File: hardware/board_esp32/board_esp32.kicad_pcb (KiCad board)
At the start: 2 copper layers, 93 parts, among them J1 USB_B_Micro, J2 Conn_01x02, J3 Micro_SD_Card_Det_Hirose_DM3AT, Q1 AO3401, Q2 AO3400, Q3 AO3401, SW1 SW_Push, U1 FT231XS, U2 ESP32-WROOM-32D, U3 E22-900M22S, U4 E22-900M30S, U5 TPS62162DGK

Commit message: adds changelog and pcb components are organised
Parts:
- removed C11: NC, Capacitor_SMD:C_0805_2012Metric
- moved Q2 131.8 mm to (255.5, 71.2), turned to 90 degrees
- moved J2 73.4 mm to (265.0, 66.0)
- moved J1 67.9 mm to (261.8, 50.5), turned to 90 degrees
- moved C1 62.6 mm to (256.2, 49.0), turned to 90 degrees
- moved C2 62.2 mm to (256.2, 51.2), turned to -90 degrees
- moved D1 61.4 mm to (257.5, 51.2), turned to -90 degrees
- moved R2 61.0 mm to (254.5, 50.8)
- moved R1 60.9 mm to (254.5, 49.5)
- moved Q3 59.6 mm to (259.5, 67.2)
- moved R6 59.4 mm to (256.5, 67.7), turned to 90 degrees
- moved D3 58.9 mm to (257.5, 53.5), turned to -90 degrees
- moved D2 58.6 mm to (257.5, 49.0)
- moved JP3 58.5 mm to (237.5, 46.0)
- moved JP4 57.9 mm to (237.5, 43.0)
- moved Q1 57.8 mm to (252.5, 67.2)
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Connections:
- SW1 pad 2: GND -> /SW_RESET

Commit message: finishes placement and starts routing
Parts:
- added H1: MountingHole_Pad, MountingHole:MountingHole_2.2mm_M2, F.Cu at (13.0, 13.0)
- added H2: MountingHole_Pad, MountingHole:MountingHole_2.2mm_M2, F.Cu at (62.0, 87.0)
- added H3: MountingHole_Pad, MountingHole:MountingHole_2.2mm_M2, F.Cu at (13.0, 87.0)
- added H4: MountingHole_Pad, MountingHole:MountingHole_2.2mm_M2, F.Cu at (62.0, 13.0)
- JP10, JP11, JP12, JP15, JP16, JP17, JP18, JP19, JP2, JP20, JP21, JP22, JP23, JP24, JP26, JP27, JP28, JP29, JP3, JP30, JP31, JP32, JP33, JP4, JP5, JP6, JP7, JP8, JP9, TP1, TP2, TP3, TP4: moved to B.Cu
- moved D5 232.9 mm to (13.0, 19.0), turned to 180 degrees
- moved R12 229.0 mm to (16.0, 19.0), turned to 0 degrees
- moved D4 228.8 mm to (13.0, 25.0), turned to 180 degrees
- moved R11 225.0 mm to (16.0, 25.0), turned to 0 degrees
- moved D6 222.8 mm to (13.0, 60.0), turned to 180 degrees
- moved R15 219.3 mm to (16.0, 60.0), turned to 0 degrees
- moved JP2 206.6 mm to (46.0, 33.0), turned to 180 degrees
- moved J2 203.2 mm to (62.0, 58.0)
- moved C7 202.9 mm to (52.5, 55.5)
- moved Q1 202.9 mm to (50.0, 55.0)
- moved Q2 202.9 mm to (53.0, 59.0)
- moved Q3 202.9 mm to (57.0, 55.0)
- moved R6 202.9 mm to (54.0, 55.5)
- moved R7 202.9 mm to (53.5, 53.5)
- moved J1 199.5 mm to (62.3, 45.0)
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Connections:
- SW1 pad 2: /SW_RESET -> GND
- U2 pad 10: /LORA1_RXEN -> /LORA1_TXEN
- U2 pad 12: /LORA1_TXEN -> /LORA1_RXEN
- U2 pad 27: /LORA1_DIO2 -> /LORA1_NSS
- U2 pad 33: /LORA1_NSS -> /LORA1_DIO2
- U2 pad 36: /LORA2_NSS -> /LORA1_BUSY
- U2 pad 6: /LORA1_BUSY -> /LORA2_NSS
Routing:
- net /LORA1_SCK: track 0.00 -> 54.7 mm, vias 0 -> 1
- net /LORA1_TXEN: track 0.00 -> 37.8 mm, vias 0 -> 1
- net /LORA1_RXEN: track 0.00 -> 37.2 mm, vias 0 -> 1
- net /ESP_LED: track 0.00 -> 28.5 mm
- net /FT_TXD: track 0.00 -> 21.7 mm, vias 0 -> 1
- net /LORA1_DIO1: track 0.00 -> 18.8 mm, vias 0 -> 1
- net /LORA1_DIO2: track 0.00 -> 18.6 mm, vias 0 -> 1
- net /FT_RXD: track 0.00 -> 15.5 mm, vias 0 -> 3
- net +3V3: track 0.00 -> 14.9 mm
- net /LORA1_MOSI: track 0.00 -> 12.6 mm, vias 0 -> 2
- net Net-(R13-Pad2): track 0.00 -> 10.8 mm
- net /LORA1_MISO: track 0.00 -> 9.51 mm, vias 0 -> 1
- net Net-(JP19-Pad2): track 0.00 -> 7.71 mm, vias 0 -> 1
- net /FT_DTR: track 0.00 -> 6.62 mm, vias 0 -> 1
- net Net-(JP18-Pad2): track 0.00 -> 5.71 mm, vias 0 -> 1
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- added copper zone on B.Cu, net GND
- added copper zone on F.Cu, net GND
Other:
- board outline added: 55 x 80 mm

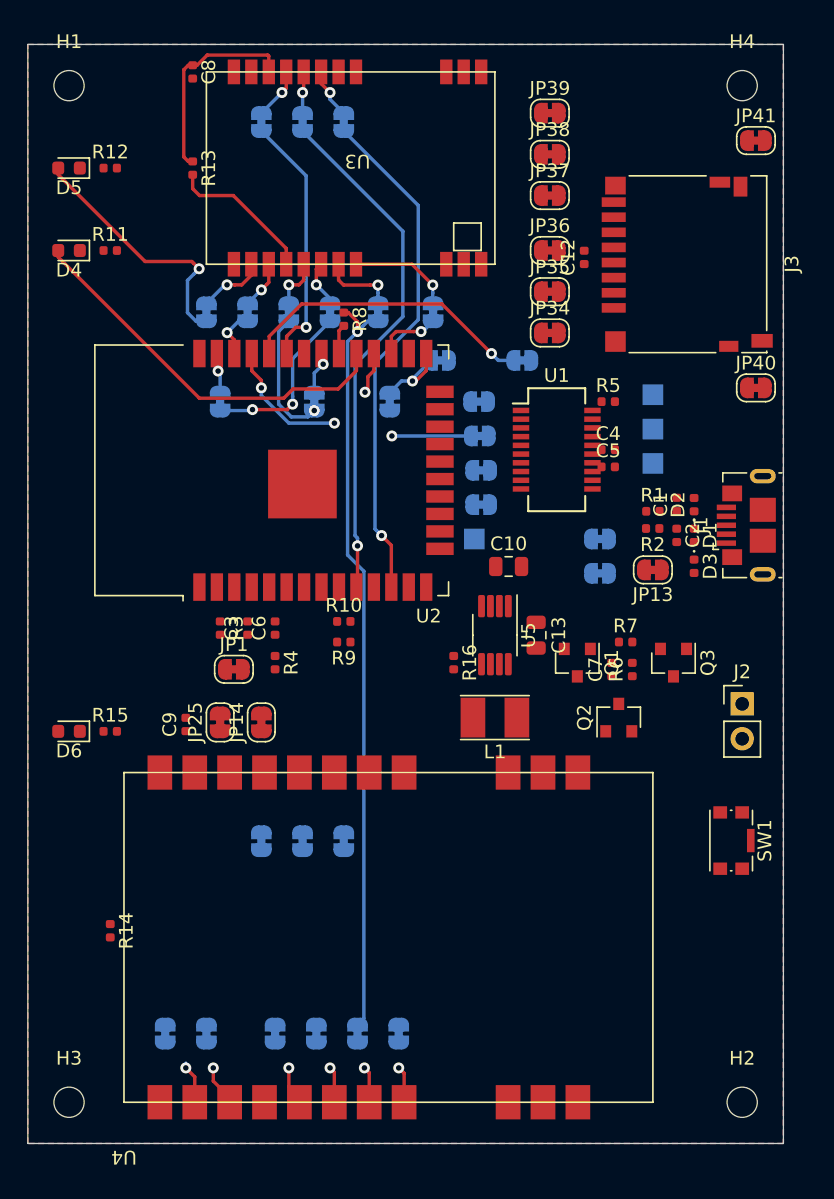
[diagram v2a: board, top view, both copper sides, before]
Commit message: finishes up layout of board_esp32
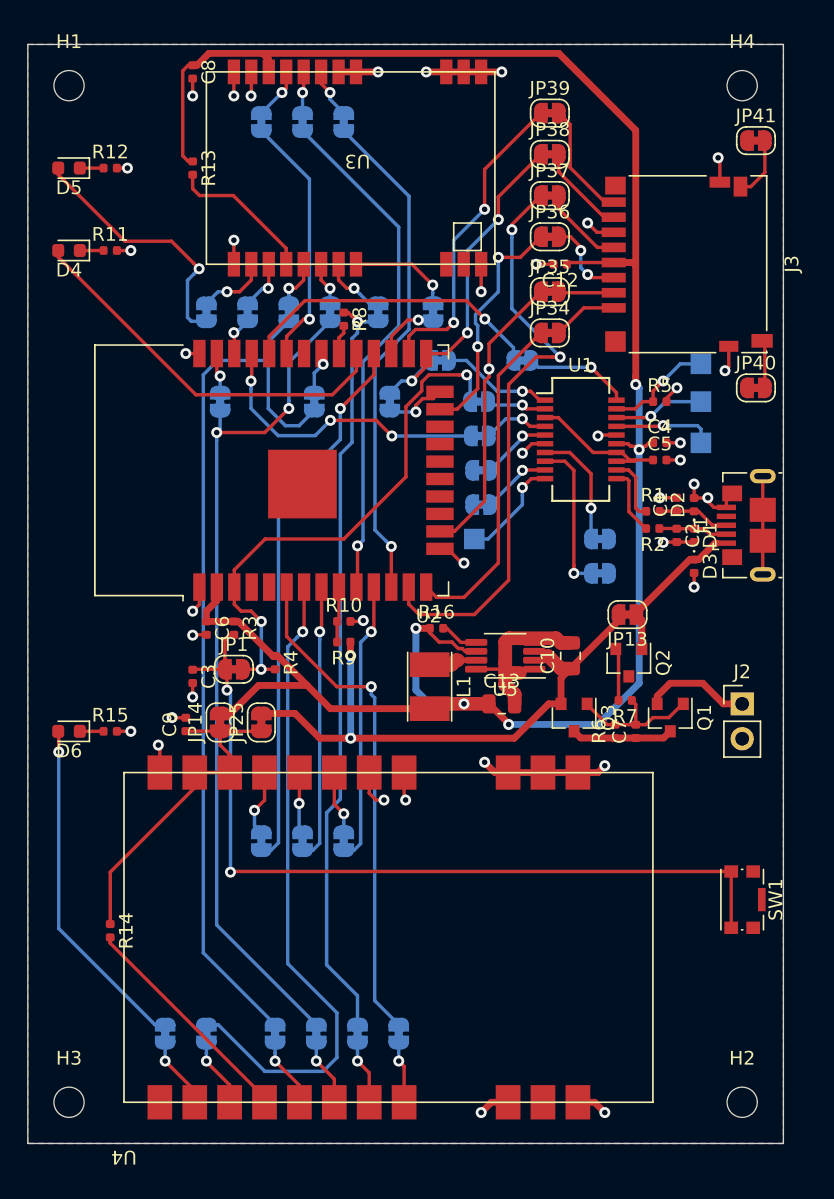
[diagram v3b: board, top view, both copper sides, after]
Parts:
- SW1: value SW_Push -> SW_Push-Std
- moved Q3 8.27 mm to (49.8, 59.0)
- moved TP4 8.05 mm to (59.0, 33.2)
- moved C10 7.91 mm to (49.5, 54.5), turned to 90 degrees
- moved Q1 7.86 mm to (56.8, 59.0)
- moved C13 5.59 mm to (44.5, 58.0), turned to 0 degrees
- moved C3 5.32 mm to (22.0, 56.0), turned to -90 degrees
- moved L1 5.26 mm to (39.2, 56.8), turned to -90 degrees
- moved C6 5.00 mm to (23.0, 52.5), turned to -90 degrees
- moved C7 4.83 mm to (54.2, 60.0)
- moved R6 4.67 mm to (52.8, 60.0)
- moved SW1 4.37 mm to (62.0, 72.2)
- moved R7 4.25 mm to (53.5, 57.8), turned to 180 degrees
- moved Q2 4.07 mm to (53.8, 55.0), turned to -90 degrees
- moved C4 3.78 mm to (56.0, 39.0)
- moved C5 3.78 mm to (56.0, 40.2)
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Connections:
- net Net-(C7-Pad1) renamed /BATT_PROT
- net Net-(J2-Pad1) renamed /BATT_IN
- J3 pad 11: Net-(J3-Pad11) -> GND
- SW1 pad 2: GND -> /SW_RESET
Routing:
- net +3V3: track 14.9 -> 152.9 mm, vias 0 -> 5
- net GND: track 0.00 -> 95.4 mm, vias 0 -> 39
- net /SW_RESET: track 0.00 -> 60.8 mm, vias 0 -> 2
- net /LORA1_MISO: track 9.51 -> 65.9 mm, vias 1 -> 0
- net /LORA1_MOSI: track 12.6 -> 61.4 mm
- net /LORA2_BUSY: track 0.00 -> 47.5 mm, vias 0 -> 1
- net /SD_CLK: track 0.00 -> 42.8 mm, vias 0 -> 2
- net +BATT: track 0.00 -> 41.4 mm, vias 0 -> 2
- net /FT_RTS: track 0.00 -> 39.0 mm, vias 0 -> 3
- net /LORA2_DIO2: track 3.08 -> 40.0 mm
- net /LORA2_NSS: track 0.00 -> 36.7 mm, vias 0 -> 1
- net /LORA2_DIO1: track 0.00 -> 25.0 mm, vias 0 -> 1
- net Net-(C9-Pad1): track 0.00 -> 24.9 mm
- net /SD_DAT2: track 0.00 -> 24.6 mm
- net /SD_DAT1: track 0.00 -> 22.8 mm, vias 0 -> 2
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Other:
- net class Default: clearance 0.2 -> 0.15
- net class PWR added: clearance 0.2, trace_width 0.25, via_dia 0.8, via_drill 0.4
- rule trace_clearance: 0.2 -> 0.15
- rule trace_min: 0.2 -> 0.15

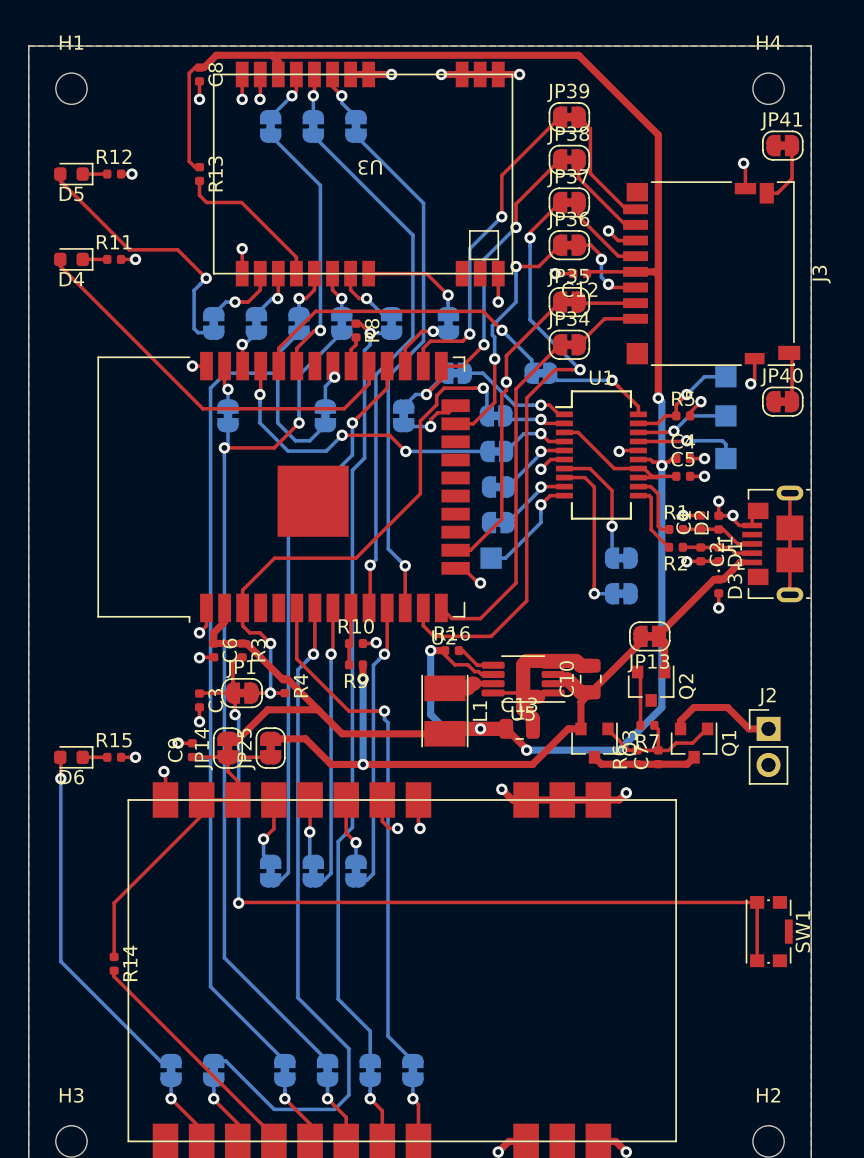
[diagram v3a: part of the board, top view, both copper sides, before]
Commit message: add a few more vias and generates GERBERs for board_esp32
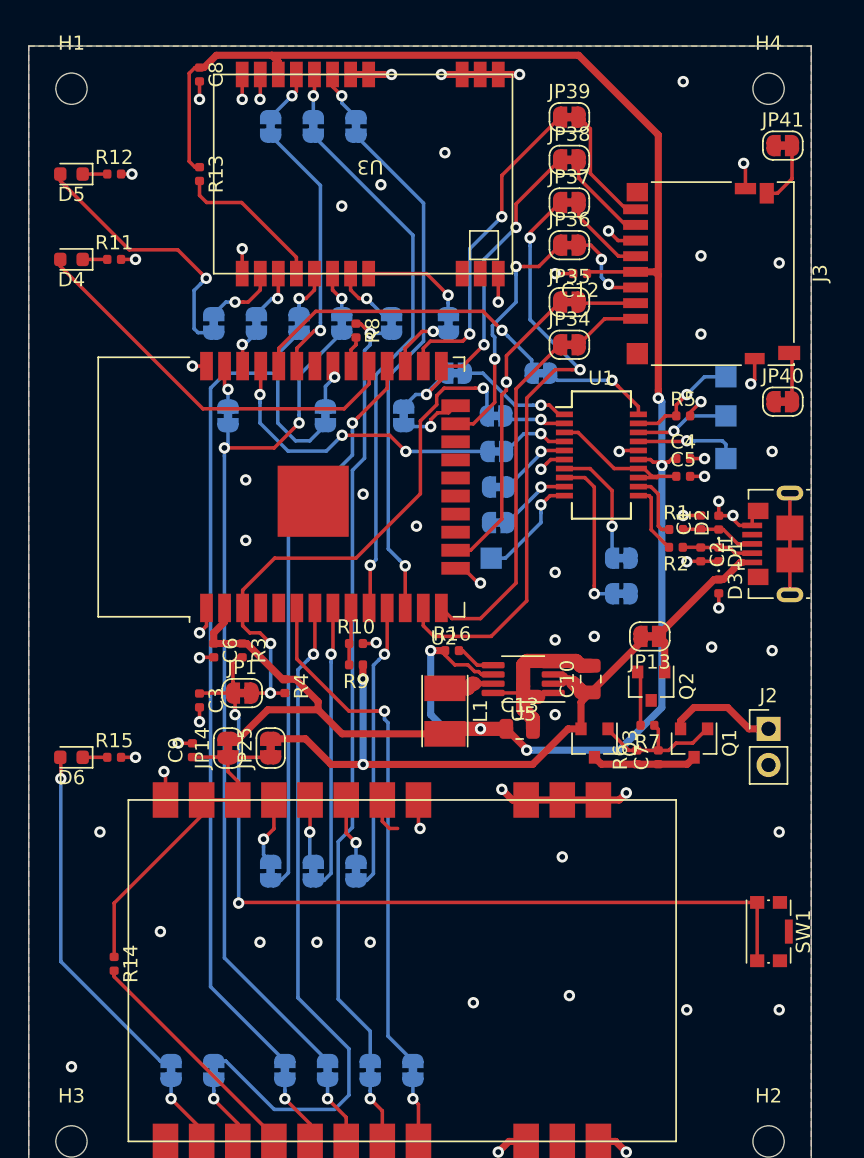
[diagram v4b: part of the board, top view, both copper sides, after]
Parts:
- U5: footprint Package_SO:MSOP-8_3x3mm_P0.65mm -> parts:MSOP-8_3x3mm_P0.65mm
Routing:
- net +BATT: track 41.4 -> 45.1 mm
- net GND: vias 39 -> 68

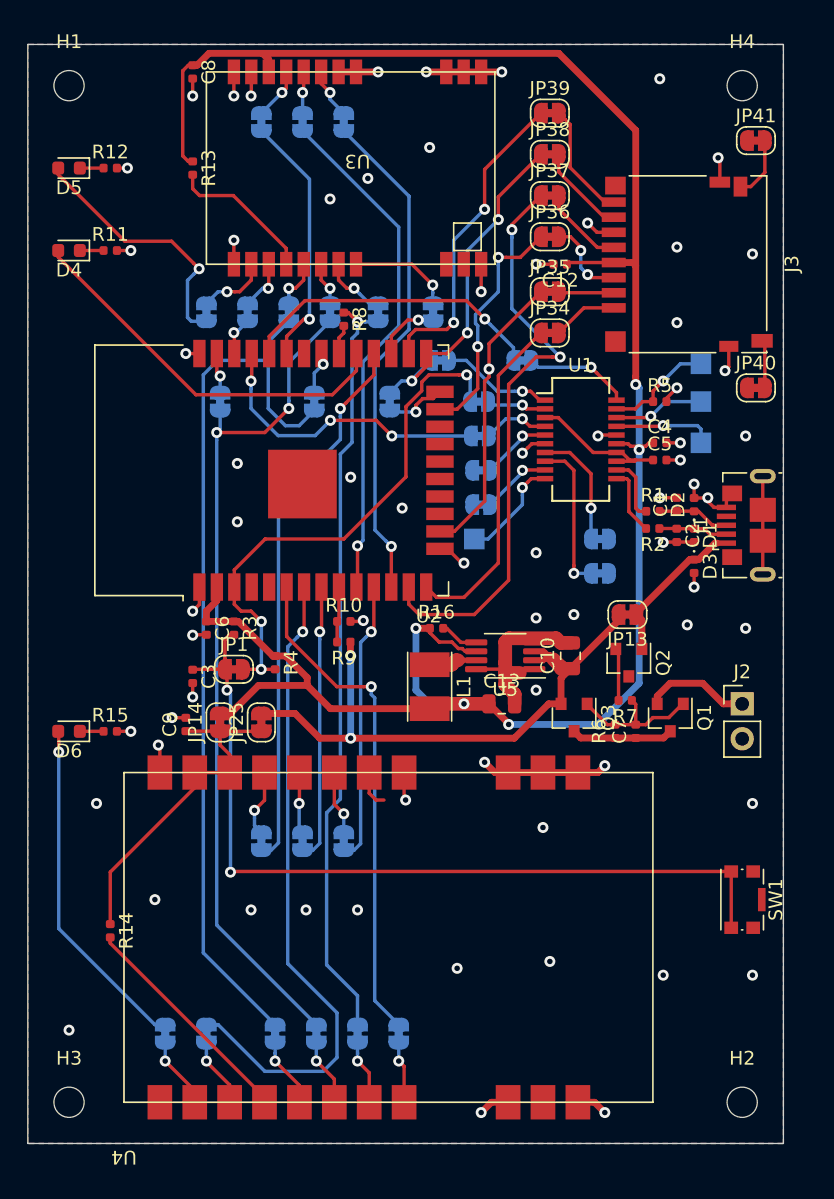
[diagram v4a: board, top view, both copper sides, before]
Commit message: updates board_esp32 to fix manufacture issue with annular ring size
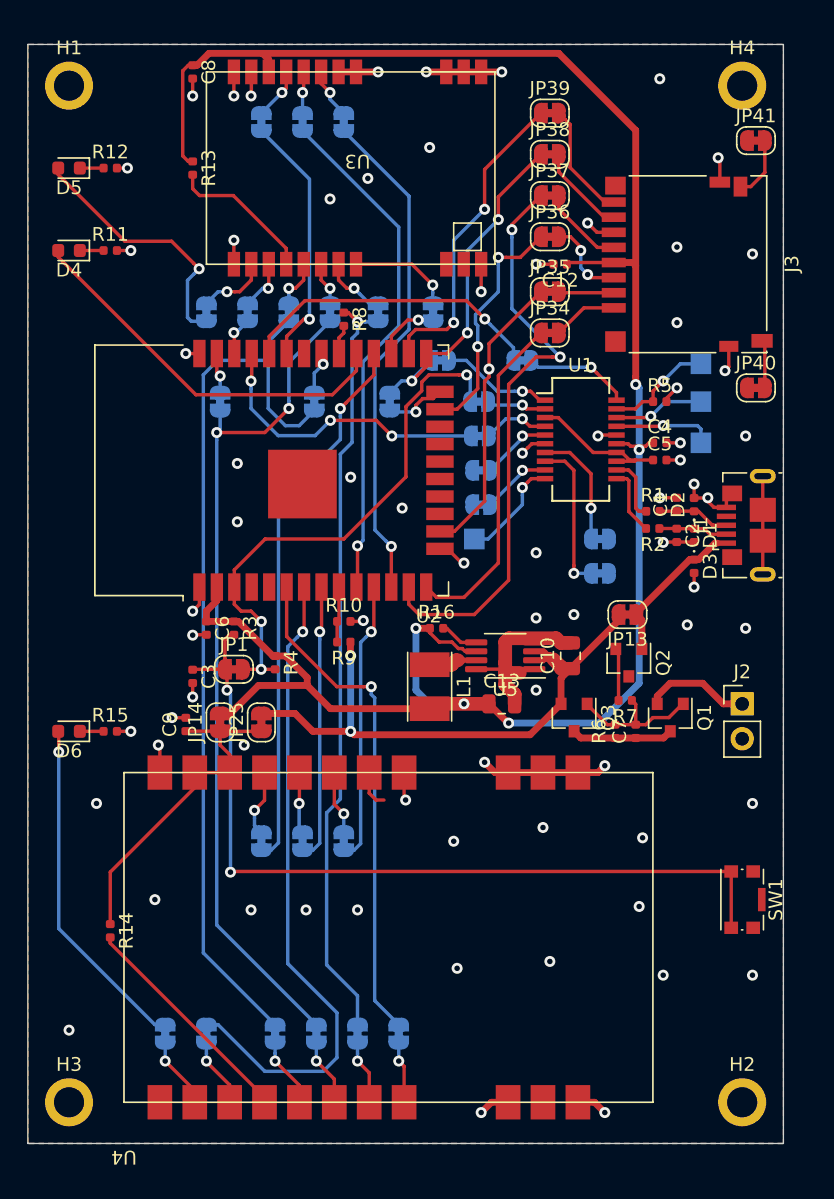
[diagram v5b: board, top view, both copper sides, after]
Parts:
- H1, H2, H3, H4: footprint MountingHole:MountingHole_2.2mm_M2 -> MountingHole:MountingHole_2.2mm_M2_ISO7380_Pad
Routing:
- net +BATT: track 45.1 -> 43.9 mm
- net GND: vias 68 -> 72
